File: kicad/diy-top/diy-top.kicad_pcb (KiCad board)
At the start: 2 copper layers, 40.6 x 82.5 mm, 17 parts

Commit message: modified:   kicad/diy-top/diy-top.kicad_pro
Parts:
- removed PMW3901_L1, PMW3901_R1: Conn_01x04_Female, Connector_PinSocket_2.54mm:PinSocket_1x04_P2.54mm_Vertical
- removed PMW3901_PWR1: Conn_01x02_Female, Connector_PinHeader_2.54mm:PinHeader_1x02_P2.54mm_Vertical
- removed VL53L1_R1: Conn_01x03_Female, Connector_PinHeader_2.54mm:PinHeader_1x03_P2.54mm_Vertical
- added J1: Conn_01x15_MountingPin, Connector_IDC:IDC-Header_2x15_P2.54mm_Vertical, F.Cu at (164.3, 116.3)
- added J1: Conn_01x15_MountingPin, Connector_IDC:IDC-Header_2x15_P2.54mm_Vertical, F.Cu at (164.0, 88.5)
- moved GND_PAD21 53.4 mm to (126.7, 98.6), turned to -90 degrees
- moved GND_PAD20 50.0 mm to (129.2, 98.4), turned to -90 degrees
- moved GND_PAD18 46.5 mm to (131.7, 98.6), turned to -90 degrees
- moved GND_PAD19 41.5 mm to (135.2, 98.5), turned to -90 degrees
- moved PMW3901_PWR2 31.0 mm to (146.1, 102.4)
- moved Motor5 31.0 mm to (160.3, 103.6)
- moved VL53L1_L5 20.9 mm to (124.4, 121.0)
- moved VL53L1_L4 16.7 mm to (120.9, 85.8)
- moved REG1 13.4 mm to (136.8, 113.4), turned to -90 degrees
- moved VL53L1_L3 12.6 mm to (170.9, 117.5)
- moved GND_PAD1 10.4 mm to (145.4, 119.2)
- moved VB_PAD1 10.4 mm to (151.9, 119.2)
- moved VL53L1_L2 5.82 mm to (167.4, 84.9)
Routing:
- net /GND: track 144.4 -> 0.30 mm, vias 2 -> 0
- net /VBAT: track 128.0 -> 0.10 mm
- net /3V3: track 84.1 -> 0.14 mm, vias 1 -> 0
- net /5V: track 53.7 -> 0.37 mm, vias 2 -> 0
- net /TX5: track 34.6 -> 0.00 mm, vias 1 -> 0
- net /RX5: track 30.8 -> 0.00 mm, vias 1 -> 0
- net /SCL0: track 17.1 -> 0.00 mm, vias 1 -> 0
- net /M2: track 10.5 -> 0.00 mm, vias 1 -> 0
- net /SCK: track 10.2 -> 0.00 mm, vias 1 -> 0
- net /M4: track 10.2 -> 0.00 mm
- net /M1: track 7.06 -> 0.19 mm
- net /SDA0: track 2.86 -> 0.00 mm, vias 2 -> 0
- net /SDA1: track 0.51 -> 0.00 mm
- net /SCL1: track 0.51 -> 0.00 mm
- removed copper zone on F.Cu, net /GND
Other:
- board outline removed
- board text removed: "3V"
- board text removed: "PMW3901"
- board text removed: "VL53L1"

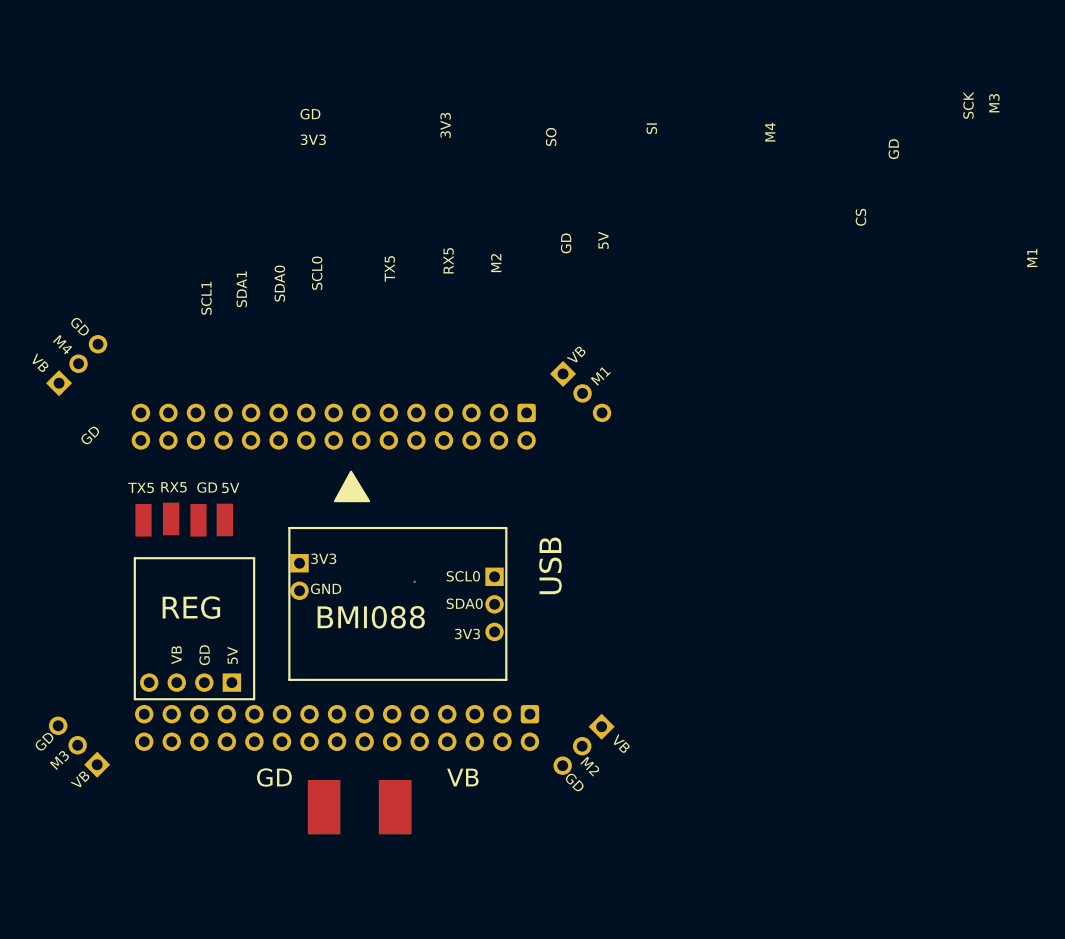
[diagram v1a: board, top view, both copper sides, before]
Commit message: modified:   kicad/diy-bottom/diy-bottom.kicad_sch
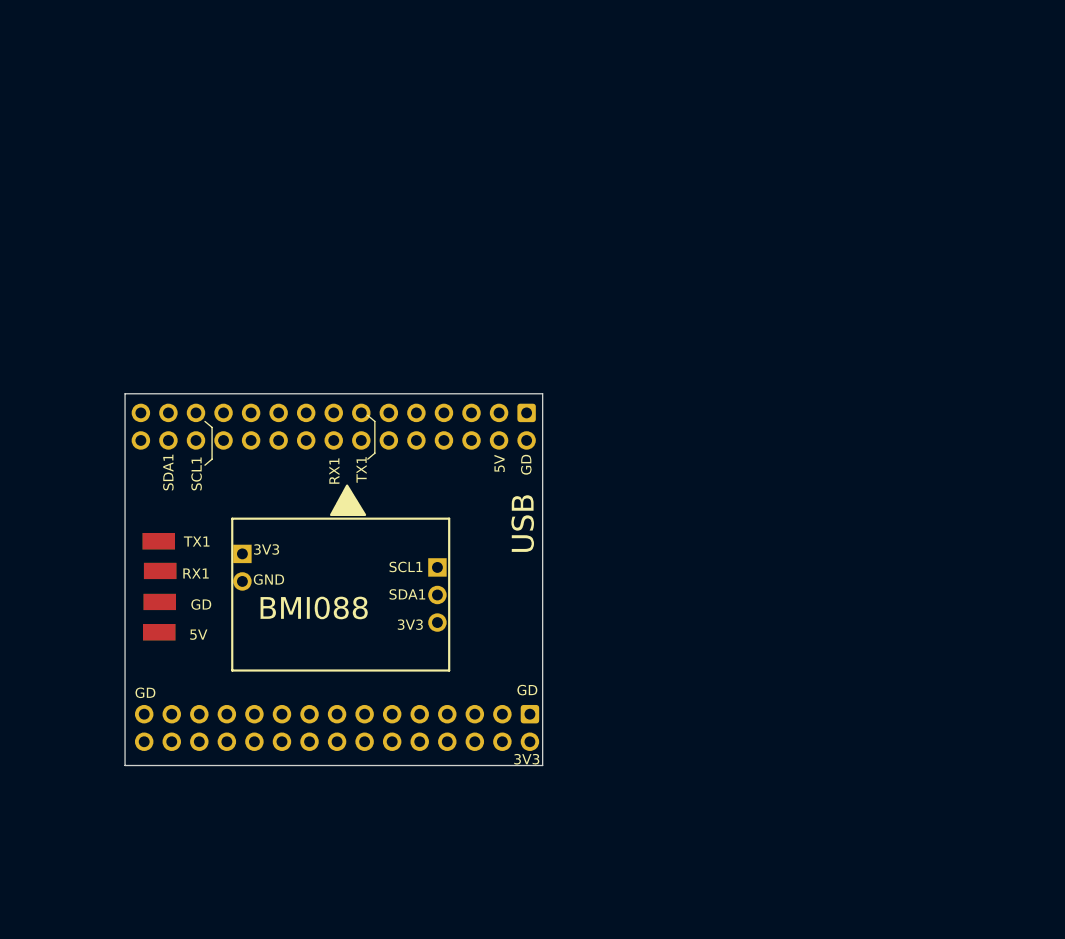
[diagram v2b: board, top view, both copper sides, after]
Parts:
- removed GND_PAD1, VB_PAD1: Conn_01x01, Connector_Wire:SolderWirePad_1x01_SMD_5x10mm
- removed REG1: Conn_01x04_Female, Connector_PinSocket_2.54mm:PinSocket_1x04_P2.54mm_Vertical
- removed VL53L1_L2, VL53L1_L3, VL53L1_L4, VL53L1_L5: Conn_01x03_Female, Connector_PinHeader_2.54mm:PinHeader_1x03_P2.54mm_Vertical
- moved GND_PAD19 12.3 mm to (130.3, 109.7), turned to 0 degrees
- moved GND_PAD18 9.50 mm to (130.4, 108.0), turned to 0 degrees
- moved GND_PAD20 6.83 mm to (130.3, 105.1), turned to 0 degrees
- moved Motor5 5.34 mm to (155.1, 102.8)
- moved PMW3901_PWR2 5.34 mm to (140.8, 101.5)
- moved GND_PAD21 5.22 mm to (130.3, 102.4), turned to 0 degrees
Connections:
- GND_PAD20 pad 1: /RX5 -> /RX1
- GND_PAD21 pad 1: /TX5 -> /TX1
- J1 pad 1: (no net) -> /GND
- J1 pad 10: (no net) -> unconnected-(J1-Pin_10-Pad10)
- J1 pad 11: (no net) -> unconnected-(J1-Pin_11-Pad11)
- J1 pad 12: (no net) -> unconnected-(J1-Pin_12-Pad12)
- J1 pad 13: (no net) -> unconnected-(J1-Pin_13-Pad13)
- J1 pad 14: (no net) -> unconnected-(J1-Pin_14-Pad14)
- J1 pad 15: (no net) -> unconnected-(J1-Pin_15-Pad15)
- J1 pad 2: (no net) -> /3V3
- J1 pad 3: (no net) -> unconnected-(J1-Pin_3-Pad3)
- J1 pad 4: (no net) -> unconnected-(J1-Pin_4-Pad4)
- J1 pad 5: (no net) -> unconnected-(J1-Pin_5-Pad5)
- J1 pad 6: (no net) -> unconnected-(J1-Pin_6-Pad6)
- J1 pad 7: (no net) -> unconnected-(J1-Pin_7-Pad7)
- J1 pad 8: (no net) -> unconnected-(J1-Pin_8-Pad8)
- J1 pad 9: (no net) -> unconnected-(J1-Pin_9-Pad9)
- J1 pad 13: unconnected-(J1-Pin_13-Pad13) -> /TX1
- J1 pad 16: (no net) -> /RX1
- J1 pad 2: unconnected-(J1-Pin_2-Pad2) -> /GND
- J1 pad 25: (no net) -> /SCL1
- J1 pad 28: (no net) -> /SDA1
- J1 pad 4: unconnected-(J1-Pin_4-Pad4) -> /5V
- Motor5 pad 1: /SCL0 -> /SCL1
- Motor5 pad 2: /SDA0 -> /SDA1
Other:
- board outline added: 38.5 x 34.3 mm
- board text added: "RX1"
- board text added: "TX1"
- board text removed: "CS"
- board text removed: "M1"
- board text removed: "M2"
- board text removed: "M3"
- board text removed: "M4"
- board text removed: "REG"
- board text removed: "RX5"
- board text removed: "SCK"
- board text removed: "SCL0"
- board text removed: "SDA0"
- board text removed: "SI"
- board text removed: "SO"
- board text removed: "TX5"
- board text removed: "VB"

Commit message: modified:   kicad/diy-top/diy-top.kicad_pcb
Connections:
- J1 pad 29: (no net) -> /GND
- J1 pad 3: unconnected-(J1-Pin_3-Pad3) -> /GND
- J1 pad 4: unconnected-(J1-Pin_4-Pad4) -> /3V3
- J1 pad 5: unconnected-(J1-Pin_5-Pad5) -> /GND
- J1 pad 6: unconnected-(J1-Pin_6-Pad6) -> /3V3
- J1 pad 1: unconnected-(J1-Pin_1-Pad1) -> /GND
- J1 pad 3: unconnected-(J1-Pin_3-Pad3) -> /5V
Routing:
- net /5V: track 0.00 -> 58.8 mm
- net /3V3: track 0.14 -> 48.6 mm
- net /GND: track 0.00 -> 41.4 mm
- net /SDA1: track 0.00 -> 31.7 mm, vias 0 -> 1
- net (no net): track 0.00 -> 26.0 mm
- net /TX1: track 0.00 -> 25.6 mm, vias 0 -> 1
- net /RX1: track 0.00 -> 21.0 mm
- added copper zone on F.Cu, net /GND
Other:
- board size 38.5 x 34.3 mm -> 40 x 34.3 mm

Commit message: modified:   kicad/diy-top/diy-top.kicad_pcb
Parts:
- moved GND_PAD18 31.5 mm to (161.9, 108.5)
- moved GND_PAD19 31.5 mm to (161.8, 110.2)
- moved GND_PAD21 31.5 mm to (161.8, 102.9)
- moved GND_PAD20 31.5 mm to (161.9, 105.6)
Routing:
- net /3V3: track 48.6 -> 6.64 mm
- net /5V: track 58.8 -> 24.2 mm
- net /SDA1: track 31.7 -> 0.12 mm, vias 1 -> 0
- net (no net): track 26.0 -> 0.00 mm
- net /TX1: track 25.6 -> 0.00 mm, vias 1 -> 0
- net /RX1: track 21.0 -> 0.00 mm
- net /GND: track 41.4 -> 33.0 mm
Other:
- outline, holes or cut-outs redrawn
- board text added: "CL1"
- board text added: "DA1"

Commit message: modified:   kicad/diy-bottom/diy-bottom.kicad_pcb
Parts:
- added D1: LED, LED_THT:LED_D3.0mm, F.Cu at (143.4, 111.9)
- added R1: R, Resistor_THT:R_Axial_DIN0204_L3.6mm_D1.6mm_P5.08mm_Horizontal, F.Cu at (150.2, 111.9)
- moved Motor5 3.79 mm to (155.1, 99.0)
- moved PMW3901_PWR2 3.79 mm to (140.8, 97.7)
- moved GND_PAD18 2.95 mm to (161.9, 111.5)
- moved GND_PAD19 2.95 mm to (161.8, 113.2)
- moved GND_PAD20 2.95 mm to (161.8, 108.6)
- moved GND_PAD21 2.95 mm to (161.8, 105.8)
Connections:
- J1 pad 10: unconnected-(J1-Pin_10-Pad10) -> /PB2
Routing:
- net /3V3: track 6.64 -> 51.6 mm
- net /SCL1: track 0.00 -> 31.6 mm
- net /SDA1: track 0.12 -> 29.3 mm, vias 0 -> 1
- net /RX1: track 0.00 -> 27.0 mm
- net /5V: track 24.2 -> 50.5 mm, vias 0 -> 1
- net /TX1: track 0.00 -> 23.0 mm
- net /GND: track 33.0 -> 47.6 mm
- net /PB2: track 0.00 -> 8.80 mm
- net Net-(D1-A): track 0.00 -> 4.19 mm
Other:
- board size 40 x 34.3 mm -> 40 x 34.2 mm
- board text removed: "CL1"
- board text removed: "DA1"
